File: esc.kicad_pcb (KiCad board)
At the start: 2 copper layers, 50 x 60.5 mm, 74 parts, among them IC1 4N25, IC2 LM25101, IC3 LM25101, IC4 LM25101, IC5 ATMEGA8-AI, P1 CONN_01X03, P2 CONN_01X03, P3 CONN_01X02, P4 CONN_02X02, P5 CONN_01X01, P6 CONN_01X01, Q1 MOSFET_N, Q10 MOSFET_N, Q11 MOSFET_N, Q12 MOSFET_N, Q2 MOSFET_N, Q3 MOSFET_N, Q4 MOSFET_N, Q5 MOSFET_N, Q6 MOSFET_N, Q7 MOSFET_N, Q8 MOSFET_N, Q9 MOSFET_N, U1 MCP1804, U2 LM2940 10V, Y1 RESONATEUR

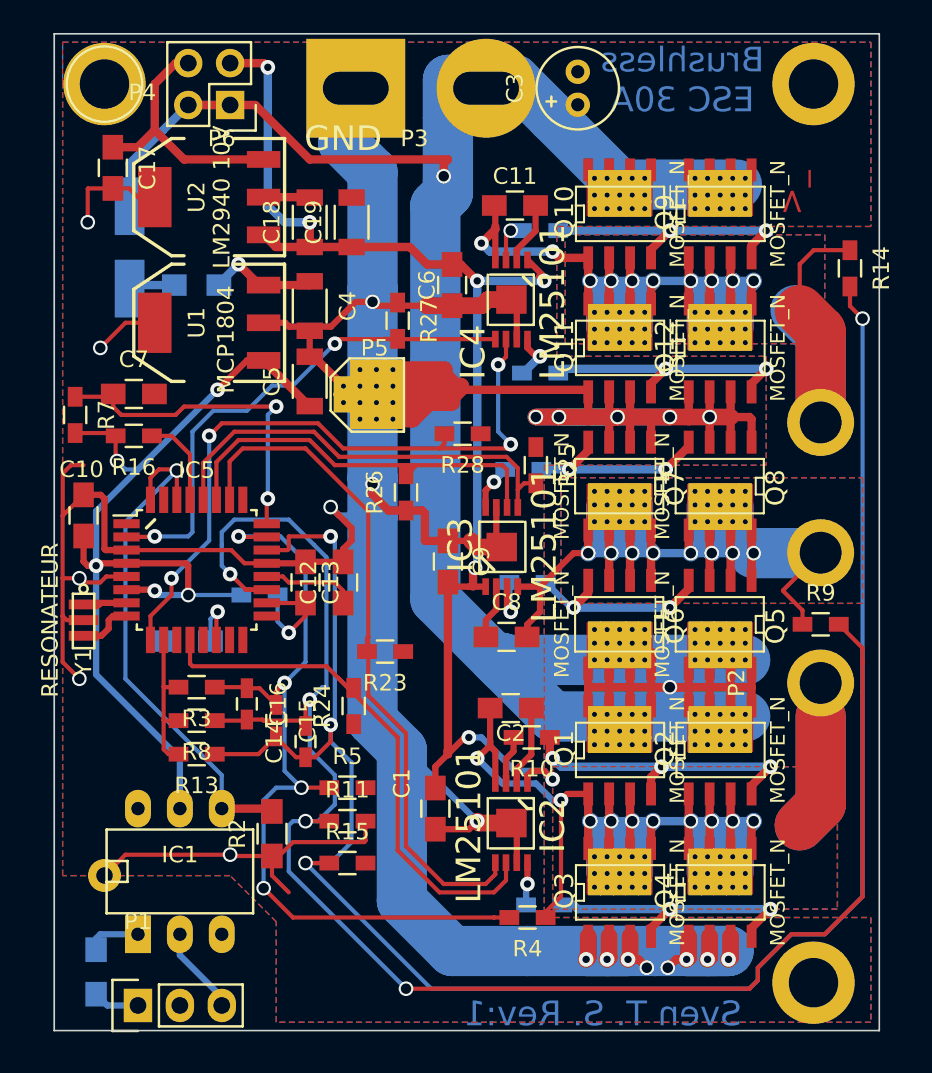
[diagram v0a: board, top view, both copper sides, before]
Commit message: Langlöcher für ausgang
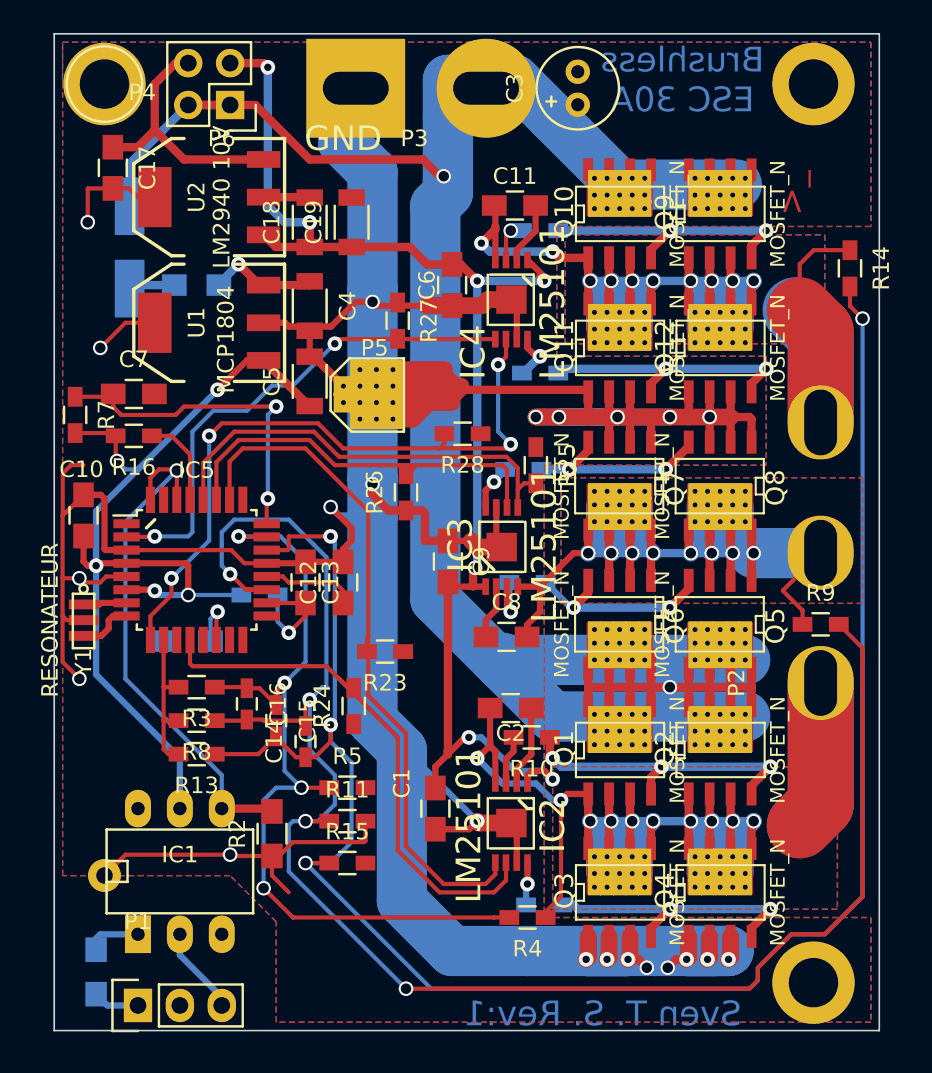
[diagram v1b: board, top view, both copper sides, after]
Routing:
- net A: track 102.5 -> 120.8 mm
- net C: track 93.4 -> 101.1 mm
- net V_BAT: track 161.9 -> 161.0 mm
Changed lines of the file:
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@@
     (thickness 1.6)
     (drawings 17)
-    (tracks 1029)
+    (tracks 1035)
     (zones 0)
     (modules 74)
@@
   )
   (setup
-    (last_trace_width 0.254)
+    (last_trace_width 4)
     (user_trace_width 0.254)
     (user_trace_width 0.381)
@@
     (user_trace_width 2.032)
     (user_trace_width 3.048)
+    (user_trace_width 4)
     (trace_clearance 0.2032)
     (zone_clearance 0.508)
@@
     (mod_text_width 0.15)
     (pad_size 4.064 4.064)
-    (pad_drill 3.048)
+    (pad_drill 2.54)
     (pad_to_mask_clearance 0)
     (aux_axis_origin 0 0)
@@
     (add_net V_BAT)
   )
+  (module Socket_Strips:Socket_Strip_Straight_1x03 (layer F.Cu)
+    (at 232.664 89.408 90)
+    (descr "Through hole socket strip")
+    (tags "socket strip")
+    (fp_text reference P2 (at 0 -5.1 90) (layer F.SilkS)
+      (effects (font (size 1 1) (thickness 0.15)))
+    )
+    (fp_text value CONN_01X03 (at 10.16 3.048 90) (layer F.Fab)
+      (effects (font (size 1 1) (thickness 0.15)))
+    )
+    (fp_line (start -1.75 -1.75) (end -1.75 1.75) (layer F.CrtYd) (width 0.05))
+    (fp_line (start 6.85 -1.75) (end 6.85 1.75) (layer F.CrtYd) (width 0.05))
+    (fp_line (start -1.75 -1.75) (end 6.85 -1.75) (layer F.CrtYd) (width 0.05))
+    (fp_line (start -1.75 1.75) (end 6.85 1.75) (layer F.CrtYd) (width 0.05))
+    (pad 1 thru_hole oval (at 0 0 90) (size 4.5 4) (drill oval 4 2) (layers *.Cu *.Mask F.SilkS)
+      (net 4 A))
+    (pad 2 thru_hole oval (at 7.9 0 90) (size 4.5 4) (drill oval 4 2) (layers *.Cu *.Mask F.SilkS)
+      (net 10 B) (zone_connect 2))
+    (pad 3 thru_hole oval (at 15.8 0 90) (size 4.5 4) (drill oval 4 2) (layers *.Cu *.Mask F.SilkS)
+      (net 12 C))
+    (model Socket_Strips.3dshapes/Socket_Strip_Straight_1x03.wrl
+      (at (xyz 0.1 0 0))
+      (scale (xyz 1 1 1))
+      (rotate (xyz 0 0 180))
+    )
+  )
   (module Socket_Strips:Socket_Strip_Straight_1x02 (layer F.Cu)
     (at 204.47 53.34)
@@
     (fp_line (start -1.75 1.75) (end 4.3 1.75) (layer F.CrtYd) (width 0.05))
     (pad 1 thru_hole rect (at 0 0) (size 6 6) (drill oval 4 2) (layers *.Cu *.Mask F.SilkS)
-      (net 2 GND))
+      (net 2 GND) (zone_connect 2))
     (pad 2 thru_hole circle (at 7.9 0) (size 6 6) (drill oval 4 2) (layers *.Cu *.Mask F.SilkS)
       (net 5 V_BAT))
@@
     )
   )
-  (module Socket_Strips:Socket_Strip_Straight_1x03 (layer F.Cu)
-    (at 232.664 89.408 90)
-    (descr "Through hole socket strip")
-    (tags "socket strip")
-    (fp_text reference P2 (at 0 -5.1 90) (layer F.SilkS)
-      (effects (font (size 1 1) (thickness 0.15)))
-    )
-    (fp_text value CONN_01X03 (at 10.16 3.048 90) (layer F.Fab)
-      (effects (font (size 1 1) (thickness 0.15)))
-    )
-    (fp_line (start -1.75 -1.75) (end -1.75 1.75) (layer F.CrtYd) (width 0.05))
-    (fp_line (start 6.85 -1.75) (end 6.85 1.75) (layer F.CrtYd) (width 0.05))
-    (fp_line (start -1.75 -1.75) (end 6.85 -1.75) (layer F.CrtYd) (width 0.05))
-    (fp_line (start -1.75 1.75) (end 6.85 1.75) (layer F.CrtYd) (width 0.05))
-    (pad 1 thru_hole circle (at 0 0 90) (size 4.064 4.064) (drill 2.54) (layers *.Cu *.Mask F.SilkS)
-      (net 4 A))
-    (pad 2 thru_hole circle (at 7.9 0 90) (size 4.064 4.064) (drill 2.54) (layers *.Cu *.Mask F.SilkS)
-      (net 10 B))
-    (pad 3 thru_hole circle (at 15.8 0 90) (size 4.064 4.064) (drill 2.54) (layers *.Cu *.Mask F.SilkS)
-      (net 12 C))
-    (model Socket_Strips.3dshapes/Socket_Strip_Straight_1x03.wrl
-      (at (xyz 0.1 0 0))
-      (scale (xyz 1 1 1))
-      (rotate (xyz 0 0 180))
-    )
-  )
   (module Connect:1pin (layer F.Cu)
     (at 204.724 73.406)
@@
   (segment (start 215.118 93.746) (end 215.118 90.932) (width 0.381) (layer F.Cu) (net 3))
   (segment (start 214.23376 94.63024) (end 215.118 93.746) (width 0.381) (layer F.Cu) (net 3))
+  (segment (start 232.664 89.408) (end 232.664 96.774) (width 4) (layer B.Cu) (net 4))
+  (segment (start 232.664 96.774) (end 231.394 98.044) (width 4) (layer B.Cu) (net 4))
+  (segment (start 232.664 96.774) (end 231.394 98.044) (width 3.048) (layer B.Cu) (net 4))
+  (segment (start 232.664 89.408) (end 232.664 96.774) (width 4) (layer F.Cu) (net 4))
+  (segment (start 232.664 96.774) (end 231.394 98.044) (width 4) (layer F.Cu) (net 4))
   (segment (start 232.664 96.774) (end 231.394 98.044) (width 3.048) (layer F.Cu) (net 4))
   (segment (start 232.664 91.44) (end 232.664 96.774) (width 3.048) (layer F.Cu) (net 4))
-  (segment (start 232.664 96.774) (end 231.394 98.044) (width 3.048) (layer B.Cu) (net 4))
   (segment (start 232.664 91.44) (end 232.664 96.774) (width 3.048) (layer B.Cu) (net 4))
   (segment (start 228.092 100.965) (end 228.092 99.949) (width 1.016) (layer B.Cu) (net 4))
@@
   (segment (start 217.297 96.139) (end 218.567 96.139) (width 0.381) (layer F.Cu) (net 4))
   (segment (start 215.392 95.504) (end 216.408 96.52) (width 0.381) (layer B.Cu) (net 4))
+  (segment (start 209.804 58.674) (end 209.55 58.674) (width 0.508) (layer F.Cu) (net 5))
+  (segment (start 209.55 58.674) (end 208.534 57.658) (width 0.508) (layer F.Cu) (net 5))
   (segment (start 196.85 54.356) (end 198.374 54.356) (width 0.508) (layer F.Cu) (net 5))
+  (segment (start 198.374 54.356) (end 201.676 57.658) (width 0.508) (layer F.Cu) (net 5))
+  (segment (start 201.676 57.658) (end 208.534 57.658) (width 0.508) (layer F.Cu) (net 5))
   (segment (start 209.804 58.674) (end 210.058 58.928) (width 0.508) (layer B.Cu) (net 5))
   (via (at 209.804 58.674) (size 0.889) (drill 0.635) (layers F.Cu B.Cu) (net 5))
-  (segment (start 209.804 57.912) (end 209.804 58.674) (width 0.508) (layer F.Cu) (net 5))
-  (segment (start 210.058 57.658) (end 209.804 57.912) (width 0.508) (layer F.Cu) (net 5))
-  (segment (start 201.676 57.658) (end 210.058 57.658) (width 0.508) (layer F.Cu) (net 5))
-  (segment (start 198.374 54.356) (end 201.676 57.658) (width 0.508) (layer F.Cu) (net 5))
   (segment (start 210.058 58.928) (end 209.55 58.928) (width 0.508) (layer B.Cu) (net 5))
   (segment (start 209.55 58.928) (end 210.058 58.928) (width 0.508) (layer B.Cu) (net 5))
@@
   (segment (start 215.372 61.996) (end 215.372 60.452) (width 0.381) (layer F.Cu) (net 11))
   (segment (start 214.23376 63.754) (end 214.23376 63.13424) (width 0.381) (layer F.Cu) (net 11))
+  (segment (start 231.394 66.802) (end 232.664 68.072) (width 4) (layer F.Cu) (net 12))
+  (segment (start 232.664 68.072) (end 232.664 73.608) (width 4) (layer F.Cu) (net 12))
+  (segment (start 232.664 73.608) (end 232.664 68.326) (width 4) (layer B.Cu) (net 12))
+  (segment (start 232.664 68.326) (end 231.14 66.802) (width 4) (layer B.Cu) (net 12))
+  (segment (start 232.664 68.326) (end 231.14 66.802) (width 3.048) (layer B.Cu) (net 12))
   (segment (start 234.442 63.162) (end 232.24 63.162) (width 0.254) (layer F.Cu) (net 12))
-  (segment (start 232.664 68.072) (end 231.394 66.802) (width 3.048) (layer F.Cu) (net 12))
   (segment (start 232.664 68.072) (end 232.664 73.608) (width 3.048) (layer F.Cu) (net 12))
   (segment (start 231.394 64.008) (end 231.394 66.802) (width 0.254) (layer F.Cu) (net 12))
   (segment (start 232.24 63.162) (end 231.394 64.008) (width 0.254) (layer F.Cu) (net 12))
-  (segment (start 232.664 73.608) (end 232.664 68.326) (width 3.048) (layer B.Cu) (net 12))
-  (segment (start 232.664 68.326) (end 231.14 66.802) (width 3.048) (layer B.Cu) (net 12))
   (segment (start 228.092 67.945) (end 228.092 66.929) (width 1.016) (layer B.Cu) (net 12))
   (segment (start 227.33 67.945) (end 227.33 66.929) (width 1.016) (layer B.Cu) (net 12))

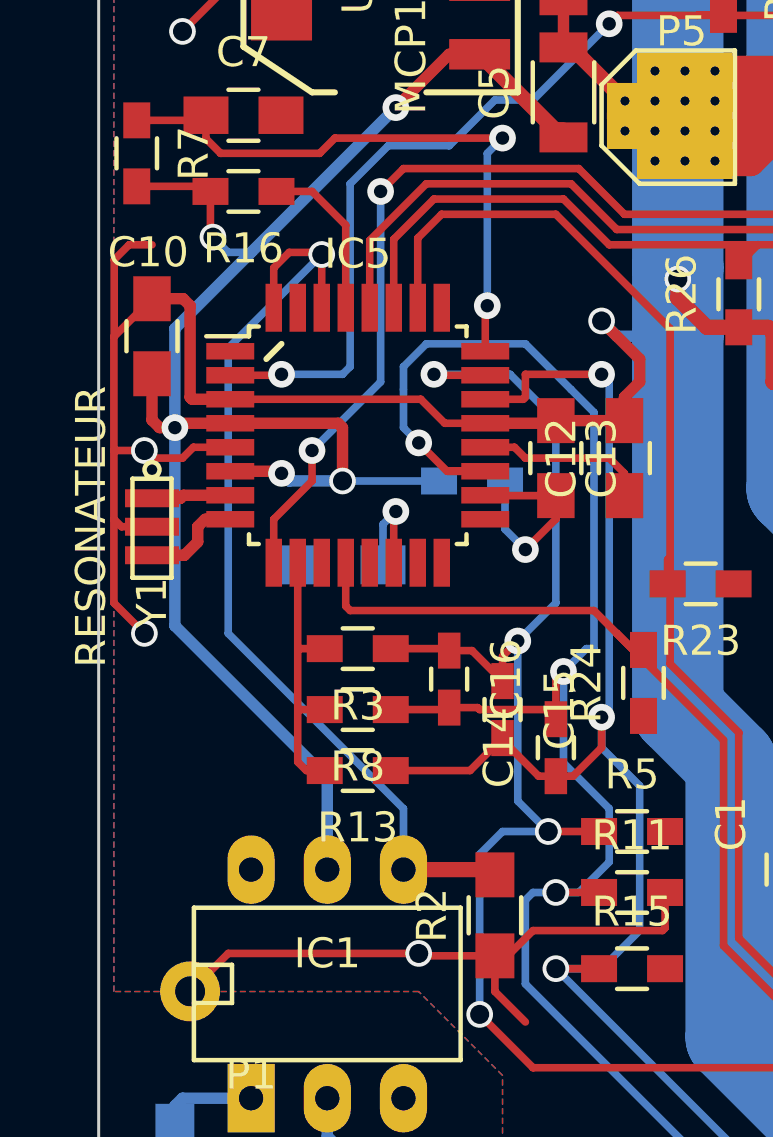
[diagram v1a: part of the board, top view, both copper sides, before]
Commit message: PWR-on LED und Fault-LED eingefügt
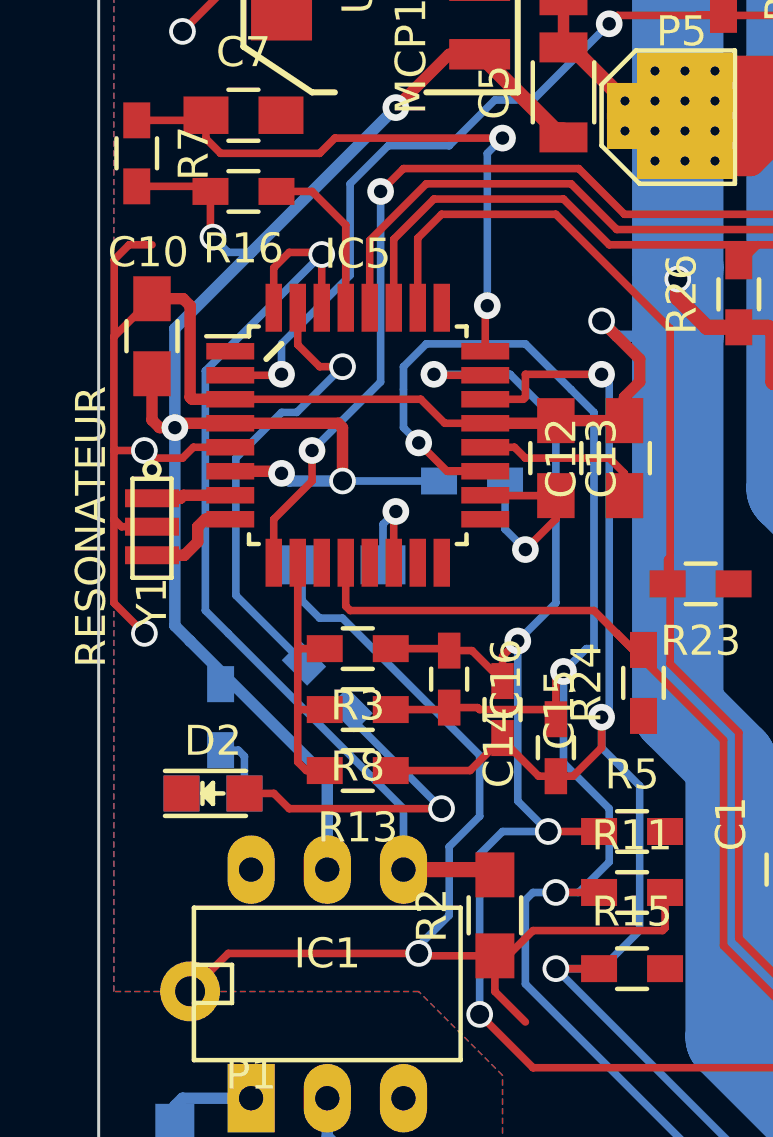
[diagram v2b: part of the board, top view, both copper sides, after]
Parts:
- added D2: LED, LEDs:LED-0805, F.Cu at (190.0, 94.5)
- added D3: LED, LEDs:LED-0805, B.Cu at (190.0, 94.5)
- added R29: 100, Resistors_SMD:R_0603_HandSoldering, B.Cu at (193.8, 90.9)
- added R30: 100, Resistors_SMD:R_0603_HandSoldering, B.Cu at (190.2, 91.9)
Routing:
- net GND: track 334.4 -> 351.1 mm
- net Net-(IC5-Pad31): track 0.00 -> 15.6 mm, vias 0 -> 1
- net Net-(D2-Pad2): track 0.00 -> 11.3 mm, vias 0 -> 1
- net Net-(D3-Pad2): track 0.00 -> 2.12 mm
- net +5V: track 62.6 -> 64.4 mm
- net C+: track 31.8 -> 30.6 mm
- net PWM: track 32.3 -> 32.9 mm

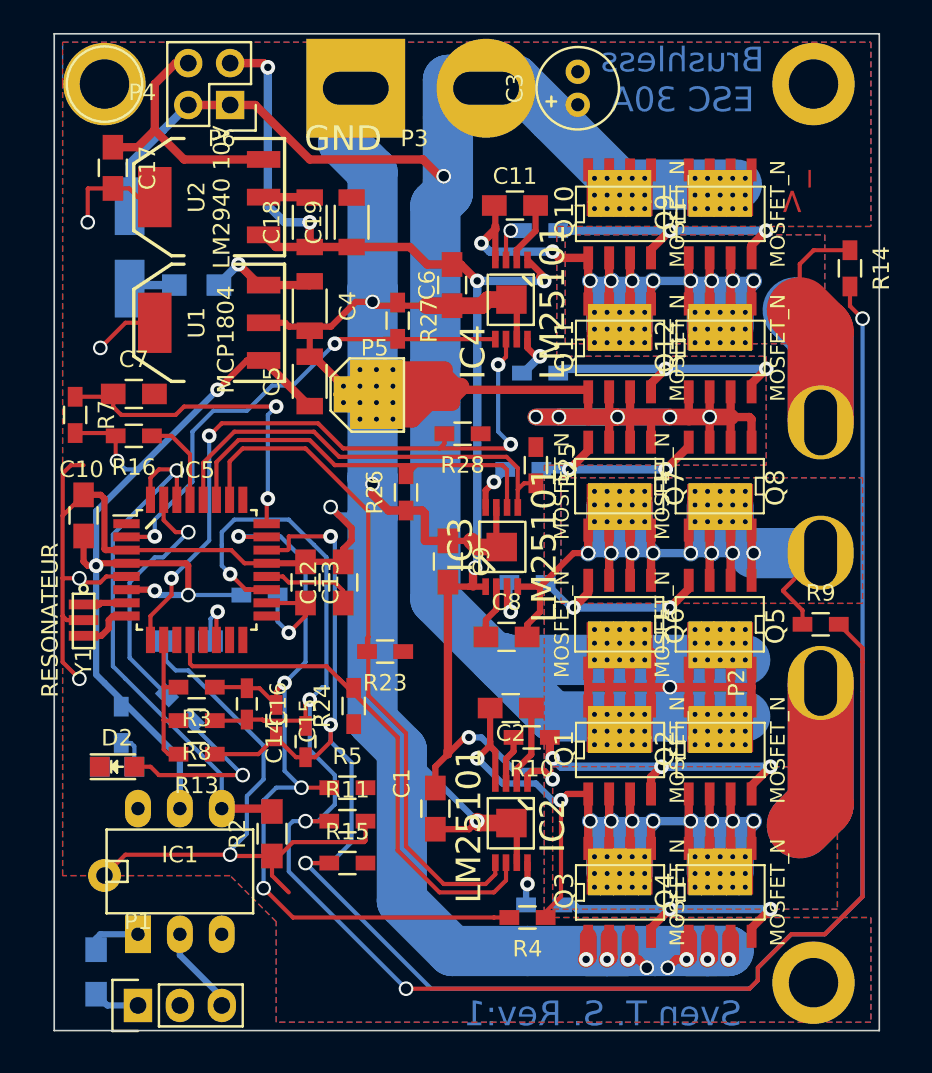
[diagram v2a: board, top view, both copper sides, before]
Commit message: FET-Pins sind jetzt auf Solid umgestellt
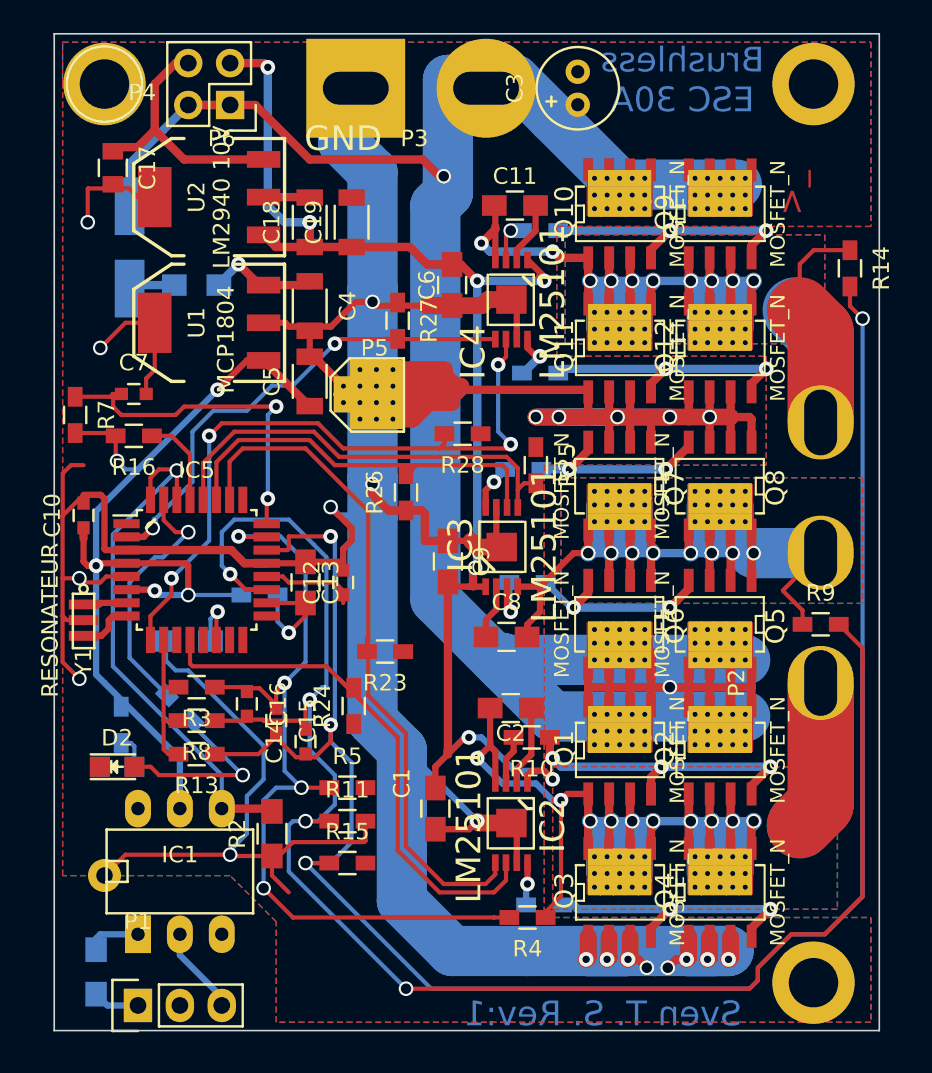
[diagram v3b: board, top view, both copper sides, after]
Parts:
- C10, C12, C7: footprint Capacitors_SMD:C_0805_HandSoldering -> Capacitors_SMD:C_0603
- C14, C15, C16: footprint Capacitors_SMD:C_0603_HandSoldering -> Capacitors_SMD:C_0603
- C17: footprint Capacitors_SMD:C_0805_HandSoldering -> Capacitors_SMD:C_0805
- Q1, Q10, Q11, Q12, Q2, Q3, Q4, Q5, Q6, Q7, Q8, Q9: footprint sven:SO8_WITH_Heatpipes -> sven:SO8_WITH_Heatpipes_New
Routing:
- net GND: track 351.1 -> 360.8 mm
- net S_PWR: track 20.8 -> 21.7 mm
- net +5V: track 64.4 -> 65.1 mm
